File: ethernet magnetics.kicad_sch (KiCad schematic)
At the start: 18 parts, among them T1 S558-5999-46-F

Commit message: did a lot more routing, phy nearly done
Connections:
- net MAG-RXn renamed MAG-RXN
- net MAG-RXp renamed MAG-RXP
- net MAG-TXn renamed MAG-TXN
- net MAG-TXp renamed MAG-TXP
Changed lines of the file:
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@@
     (stroke (width 0) (type default) (color 0 0 0 0))
   )
-  (global_label "MAG-TXp" (shape input) (at 210.82 72.39 0) (fields_autoplaced)
+  (global_label "MAG-TXP" (shape input) (at 210.82 72.39 0) (fields_autoplaced)
     (effects (font (size 1.27 1.27)) (justify left))
-    (property "Intersheet References" "${INTERSHEET_REFS}" (id 0) (at 221.9417 72.4694 0)
+    (property "Intersheet References" "${INTERSHEET_REFS}" (id 0) (at 222.0626 72.3106 0)
       (effects (font (size 1.27 1.27)) (justify left) hide)
     )
   )
-  (global_label "MAG-RXp" (shape input) (at 68.58 64.77 180) (fields_autoplaced)
+  (global_label "MAG-RXP" (shape input) (at 68.58 64.77 180) (fields_autoplaced)
     (effects (font (size 1.27 1.27)) (justify right))
-    (property "Intersheet References" "${INTERSHEET_REFS}" (id 0) (at 57.1559 64.6906 0)
+    (property "Intersheet References" "${INTERSHEET_REFS}" (id 0) (at 57.035 64.6906 0)
       (effects (font (size 1.27 1.27)) (justify right) hide)
     )
@@
     )
   )
-  (global_label "MAG-RXn" (shape input) (at 68.58 67.31 180) (fields_autoplaced)
+  (global_label "MAG-RXN" (shape input) (at 68.58 67.31 180) (fields_autoplaced)
     (effects (font (size 1.27 1.27)) (justify right))
-    (property "Intersheet References" "${INTERSHEET_REFS}" (id 0) (at 57.1559 67.2306 0)
+    (property "Intersheet References" "${INTERSHEET_REFS}" (id 0) (at 56.9745 67.2306 0)
       (effects (font (size 1.27 1.27)) (justify right) hide)
     )
@@
     )
   )
-  (global_label "MAG-TXn" (shape input) (at 210.82 74.93 0) (fields_autoplaced)
+  (global_label "MAG-TXN" (shape input) (at 210.82 74.93 0) (fields_autoplaced)
     (effects (font (size 1.27 1.27)) (justify left))
-    (property "Intersheet References" "${INTERSHEET_REFS}" (id 0) (at 221.9417 75.0094 0)
+    (property "Intersheet References" "${INTERSHEET_REFS}" (id 0) (at 222.1231 74.8506 0)
       (effects (font (size 1.27 1.27)) (justify left) hide)
     )

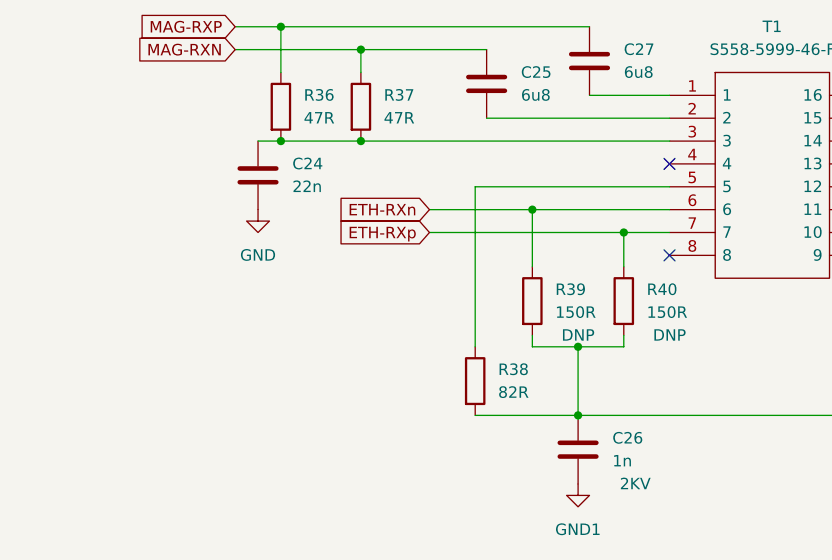
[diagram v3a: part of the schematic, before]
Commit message: tweaked power circuit, sorted drc errors and warnings, visual checked pcb
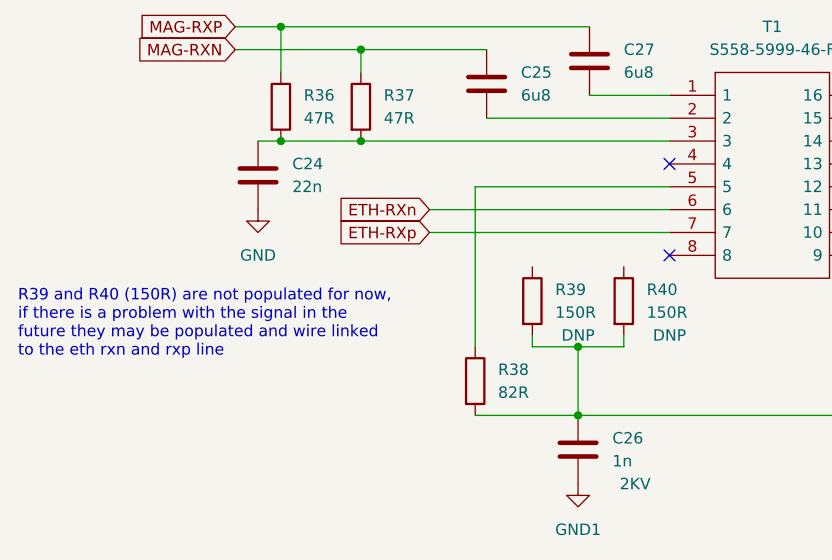
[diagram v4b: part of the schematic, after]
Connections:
- net ETH-RXn: no longer R39.1
- net ETH-RXp: no longer R40.1
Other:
- note added: "R39 and R40 (150R) are not populated for now, if there is a problem with the signal in the future they may be populated and wire linked to the eth rxn and rxp line"
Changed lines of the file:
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@@
   (junction (at 168.91 74.93) (diameter 0) (color 0 0 0 0)
-  )
-  (junction (at 111.76 87.63) (diameter 0) (color 0 0 0 0)
   )
   (junction (at 186.69 63.5) (diameter 0) (color 0 0 0 0)
   )
   (junction (at 177.8 72.39) (diameter 0) (color 0 0 0 0)
-  )
-  (junction (at 101.6 85.09) (diameter 0) (color 0 0 0 0)
   )
   (junction (at 106.68 100.33) (diameter 0) (color 0 0 0 0)
@@
     (stroke (width 0) (type default) (color 0 0 0 0))
   )
-  (wire (pts (xy 111.76 87.63) (xy 111.76 91.44))
-    (stroke (width 0) (type default) (color 0 0 0 0))
-  )
-  (wire (pts (xy 101.6 85.09) (xy 116.84 85.09))
+  (wire (pts (xy 90.17 85.09) (xy 116.84 85.09))
     (stroke (width 0) (type default) (color 0 0 0 0))
   )
   (wire (pts (xy 73.66 77.47) (xy 82.55 77.47))
-    (stroke (width 0) (type default) (color 0 0 0 0))
-  )
-  (wire (pts (xy 101.6 85.09) (xy 101.6 91.44))
     (stroke (width 0) (type default) (color 0 0 0 0))
   )
@@
     (stroke (width 0) (type default) (color 0 0 0 0))
   )
-  (wire (pts (xy 111.76 87.63) (xy 116.84 87.63))
+  (wire (pts (xy 90.17 87.63) (xy 116.84 87.63))
     (stroke (width 0) (type default) (color 0 0 0 0))
   )
@@
   )
   (wire (pts (xy 177.8 72.39) (xy 139.7 72.39))
-    (stroke (width 0) (type default) (color 0 0 0 0))
-  )
-  (wire (pts (xy 90.17 85.09) (xy 101.6 85.09))
     (stroke (width 0) (type default) (color 0 0 0 0))
   )
@@
     (stroke (width 0) (type default) (color 0 0 0 0))
   )
-  (wire (pts (xy 90.17 87.63) (xy 111.76 87.63))
-    (stroke (width 0) (type default) (color 0 0 0 0))
-  )
   (wire (pts (xy 101.6 100.33) (xy 106.68 100.33))
     (stroke (width 0) (type default) (color 0 0 0 0))
@@
     (stroke (width 0) (type default) (color 0 0 0 0))
   )
+  (text "R39 and R40 (150R) are not populated for now, \nif there is a problem with the signal in the \nfuture they may be populated and wire linked \nto the eth rxn and rxp line"
+    (at 44.45 101.6 0)
+    (effects (font (size 1.27 1.27)) (justify left bottom))
+  )
   (global_label "MAG-TXP" (shape input) (at 210.82 72.39 0) (fields_autoplaced)

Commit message: Update sourcing URLs
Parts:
- FB4: Source https://uk.farnell.com/bourns/mh3261-601y/ferrite-bead-0-1o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 -> https://onecall.farnell.com/bourns/mh3261-601y/ferrite-bead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
- T1: Source https://uk.farnell.com/stewart-connector/s558-5999-46-f/pul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 -> https://onecall.farnell.com/stewart-connector/s558-5999-46-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
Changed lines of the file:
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@@
       (effects (font (size 1.27 1.27)) (justify left) hide)
     )
-    (property "Source" "https://uk.farnell.com/stewart-connector/s558-5999-46-f/pulse-transformer-1ct-1ct-420uh/dp/2676007" (id 10) (at 116.84 72.39 0)
+    (property "Source" "https://onecall.farnell.com/stewart-connector/s558-5999-46-f/pulse-transformer-1ct-1ct-420uh/dp/2676007" (id 10) (at 116.84 72.39 0)
       (effects (font (size 1.27 1.27)) hide)
     )
@@
       (effects (font (size 1.27 1.27)) hide)
     )
-    (property "Source" "https://uk.farnell.com/bourns/mh3261-601y/ferrite-bead-0-1ohm-2a-1206/dp/27870" (id 4) (at 177.8 59.69 0)
-      (effects (font (size 1.27 1.27)) hide)
-    )
+    (property "Source" "https://onecall.farnell.com/bourns/mh3261-601y/ferrite-bead-0-1ohm-2a-1206/dp/2787025" (id 4) (at 177.8 59.69 0)
+      (effects (font (size 1.27 1.27)) hide)
+    )

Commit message: Emergency fixes
Change 6u8 cap foot print and add back copper plane
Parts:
- C25, C27: footprint Capacitor_SMD:C_0603_1608Metric_Pad1.08x0.95mm_HandSolder -> Capacitor_SMD:C_0805_2012Metric_Pad1.18x1.45mm_HandSolder
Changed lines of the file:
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@@
       (effects (font (size 1.27 1.27)) (justify left))
     )
-    (property "Footprint" "Capacitor_SMD:C_0603_1608Metric_Pad1.08x0.95mm_HandSolder" (id 2) (at 108.9152 72.39 0)
+    (property "Footprint" "Capacitor_SMD:C_0805_2012Metric_Pad1.18x1.45mm_HandSolder" (id 2) (at 108.9152 72.39 0)
       (effects (font (size 1.27 1.27)) hide)
     )
@@
       (effects (font (size 1.27 1.27)) (justify left))
     )
-    (property "Footprint" "Capacitor_SMD:C_0603_1608Metric_Pad1.08x0.95mm_HandSolder" (id 2) (at 97.4852 74.93 0)
-      (effects (font (size 1.27 1.27)) hide)
-    )
+    (property "Footprint" "Capacitor_SMD:C_0805_2012Metric_Pad1.18x1.45mm_HandSolder" (id 2) (at 97.4852 74.93 0)
+      (effects (font (size 1.27 1.27)) hide)
+    )
